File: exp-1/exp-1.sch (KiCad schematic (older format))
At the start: 15 parts

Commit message: Work continues on exp1
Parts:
- added C? (x7): .01u, symbol C
- added C? (x4): 470p, symbol C
- added C?: 15p, symbol C
- added D1: BAR15-1, Housings_SOT-23_SOT-143_TSOT-6:SOT-23, symbol DP2CA
- added FB? (x2): FILTER, symbol FILTER
- added FILT?: MTFILT, symbol MTFILT
- added L5, L? (x5): .33u, Resistors_SMD:R_0603, symbol INDUCTOR_C
- added R?: 680R, symbol R
- added R? (x2): 121R, symbol R
- added U?: ABA-52563, symbol ABA-52563
- added U?: AVT-50663, symbol AVT-50663
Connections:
- net labels added: RATT, VTX
- wire segments 24 -> 94
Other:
- note added: "NOTE: CONFIRM BIAS RESISTORS\n"
- note added: "RF BPF"
- note added: "SRSLY\n"
- moved on the sheet: C1, C10, C2, C3, C4, C5, C6, C7, C8, C9, FILT?, L1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

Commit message: More work done on copying DSP-10. Layout started.
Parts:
- added C23, C31, C38, C43: 470p, Capacitors_SMD:C_0603_HandSoldering, symbol C
- added C24, C25, C27, C32, C36, C39, C41, C44: .01u, Capacitors_SMD:C_0603_HandSoldering, symbol C
- added C26, C28, C30: 15p, Capacitors_SMD:C_0603_HandSoldering, symbol C
- added C29: 8.2p, Capacitors_SMD:C_0603_HandSoldering, symbol C
- added C33, C40: 47p, Capacitors_SMD:C_0603_HandSoldering, symbol C
- added C34, C37: 12p, Capacitors_SMD:C_0603_HandSoldering, symbol C
- added C35: 1p, Capacitors_SMD:C_0603_HandSoldering, symbol C
- added C42: 33p, Capacitors_SMD:C_0603_HandSoldering, symbol C
- added D2: BAR15-1, Housings_SOT-23_SOT-143_TSOT-6:SOT-23, symbol DP2CA
- added FILT3, FILT4: MTFILT, exp-1:FILTACH32T, symbol MTFILT
- added L11: 100n, Resistors_SMD:R_0603, symbol INDUCTOR_C
- added L12: 39n, Resistors_SMD:R_0603, symbol INDUCTOR
- added L13, L14, L15, L16, L17: .33u, Resistors_SMD:R_0603, symbol INDUCTOR_C
- added L18, L19: 100n, Resistors_SMD:R_0603, symbol INDUCTOR
- added P1, P2, P3: CONN_2, symbol CONN_2
- added Q1: 2n5109, Discret:TO39EBC, symbol NPN
- added R10, R11, R12: 331R, Resistors_SMD:R_0603_HandSoldering, symbol RA
- added R4: 3.3k, Resistors_SMD:R_0603_HandSoldering, symbol RA
- added R5: 1K, Resistors_SMD:R_0603_HandSoldering, symbol RA
- added R6: 2.2R, Resistors_SMD:R_0603_HandSoldering, symbol RA
- added R7: 22R, Resistors_SMD:R_0603_HandSoldering, symbol RA
- added R8: 680R, Resistors_SMD:R_0603_HandSoldering, symbol RA
- added R9: 121R, Resistors_SMD:R_0603_HandSoldering, symbol RA
- added U3: ABA-52563, exp-1:SOT_363, symbol ABA-52563
- added U4: AVT-50663, exp-1:SOT_363, symbol AVT-50663
- C1, C10, C2, C3, C4, C5, C6, C7, C8, C9: footprint Resistors_SMD:R_0603 -> Capacitors_SMD:C_0603_HandSoldering
- C11, C12, C13, C14, C15, C16, C17, C18, C19, C20, C21, C22: renamed from C?; footprint (none) -> Capacitors_SMD:C_0603_HandSoldering
- FB1, FB2: renamed from FB?; footprint (none) -> Choke_SMD:Choke_SMD_1206_Handsoldering
- FILT1, FILT2: renamed from FILT?; footprint (none) -> exp-1:FILTACH32T
- R1, R2: renamed from R?; footprint (none) -> Resistors_SMD:R_0603_HandSoldering; symbol R -> RA
- R3: renamed from R?; value 121R -> 331R; footprint (none) -> Resistors_SMD:R_0603_HandSoldering; symbol R -> RA
- U1, U2: renamed from U?; footprint (none) -> exp-1:SOT_363
- gave numbers to parts that had none: 5
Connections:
- net labels added: RATT2, RATT_1, TX_P, VRX
- net labels removed: RATT
- wire segments 94 -> 220
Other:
- moved on the sheet: C1, C10, C11, C12, C13, C14, C15, C16, C17, C18, C19, C2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

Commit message: Continued work on radio project thing
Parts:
- removed C20: 470p, Capacitors_SMD:C_0603_HandSoldering, symbol C
- removed C22: .01u, Capacitors_SMD:C_0603_HandSoldering, symbol C
- removed FILT2: MTFILT, exp-1:FILTACH32T, symbol MTFILT
- removed L10: .33u, Resistors_SMD:R_0603, symbol INDUCTOR_C
- removed P1: CONN_2, symbol CONN_2
- added SL?: SDRSEL, symbol SDRSEL
- added U?: ADE-1, symbol ADE-1
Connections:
- net GND: now also U?.1, U?.4, U?.5
- net TX_P: now also SL?.1; no longer P3.1 (P1)
- net at C10.1: now also U?.3 (RF)
- net at D2.1, L13.1: now also C31.2; no longer C31.1
- new net: P3.1 (P1), SL?.2
- new net IF: U?.2 (IF)
- new net LO: U?.6 (LO)
- new net TX_SL: C31.1, SL?.3
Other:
- moved on the sheet: C1, C10, C11, C12, C13, C14, C15, C16, C17, C18, C19, C2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

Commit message: Further work on radio thing
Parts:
- added U?: Si570, symbol Si570
- SL1: renamed from SL?; footprint (none) -> exp-1:BSEL2
- U5: renamed from U?; footprint (none) -> exp-1:PL-052
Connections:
- net GND: now also U?.3 (GND)
- new net +3.3V: U?.6 (VCC)

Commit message: Finished first round of routing. Power circuitry and breakout still needed.
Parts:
- added C20, C22: .01u, Capacitors_SMD:C_0603_HandSoldering, symbol C
- added C45, C46: 470p, Capacitors_SMD:C_0603_HandSoldering, symbol C
- added R13, R14: 1K, Resistors_SMD:R_0603_HandSoldering, symbol RA
- added R15: 38R, Resistors_SMD:R_0603_HandSoldering, symbol RA
- U6: renamed from U?; footprint (none) -> exp-1:SI570-HS
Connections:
- net +3.3V: now also U6.2 (OE), C20.1, C22.1, R13.2, R14.2
- net GND: now also C20.2, C22.2
- net IF: now also C46.1; no longer U5.2 (IF)
- net LO: now also C45.1
- net at C39.1, FILT4.1, R10.2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: no longer C41.1, L16.1, R9.2, U3.4 (VCC)
- net at U6.4 (CLK+): now also R15.2
- net SDA: now reaches U6.7 (SDA)
- net SDA: now also R14.1
- net SCL: now reaches U6.8 (SCL)
- net SCL: now also R13.1
- new net: C41.1, L16.1, R9.2, U3.4 (VCC)
- new net: C45.2, R15.1
- new net: C46.2, U5.2 (IF)
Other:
- note removed: "NOTE: CONFIRM BIAS RESISTORS\n"
- note removed: "SRSLY\n"
- moved on the sheet: U6

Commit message: Some more radio work
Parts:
- added Q? (x2): DMP3099L, symbol MOSFET_P
- added Q?: MMBT3904T, symbol NPN
- added Q?: NPN, symbol NPN
- added R? (x4): 10K, symbol RA
- added R? (x2): 1K, symbol RA
- added U?: LM2937, symbol LM2937
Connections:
- net GND: now also Q?.1 (E), Q?.1 (E), R?.1, R?.1, U?.2 (GND)
- net VRX: now also Q?.S
- net VTX: now also Q?.S
- new net: Q?.3 (C), Q?.G, R?.2 (x2)
- new net: Q?.2 (B), R?.2, R?.2 (x2)
- new net 10V: Q?.D, Q?.D, R?.1, R?.1, U?.3 (VO)
- new net EN_RX: R?.1
- new net EN_TX: R?.1
- new net VIN: U?.1 (VI)
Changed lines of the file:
@@
 Wire Wire Line
 	4300 5350 4600 5350
+$Comp
+L MOSFET_P Q?
+U 1 1 551F46EA
+P 2550 3500
+F 0 "Q?" H 2550 3690 60  0000 R CNN
+F 1 "DMP3099L" H 3150 3550 60  0000 R CNN
+F 2 "" H 2550 3500 60  0000 C CNN
+F 3 "" H 2550 3500 60  0000 C CNN
+	1    2550 3500
+	1    0    0    -1
+$EndComp
+$Comp
+L MOSFET_P Q?
+U 1 1 551F47CB
+P 4450 3500
+F 0 "Q?" H 4450 3690 60  0000 R CNN
+F 1 "DMP3099L" H 5050 3550 60  0000 R CNN
+F 2 "" H 4450 3500 60  0000 C CNN
+F 3 "" H 4450 3500 60  0000 C CNN
+	1    4450 3500
+	1    0    0    -1
+$EndComp
+$Comp
+L NPN Q?
+U 1 1 551F52D8
+P 2100 3750
+F 0 "Q?" H 2100 3600 50  0000 R CNN
+F 1 "MMBT3904T" H 2100 3900 50  0000 R CNN
+F 2 "" H 2100 3750 60  0000 C CNN
+F 3 "" H 2100 3750 60  0000 C CNN
+	1    2100 3750
+	1    0    0    -1
+$EndComp
+$Comp
+L NPN Q?
+U 1 1 551F5992
+P 4000 3750
+F 0 "Q?" H 4000 3600 50  0000 R CNN
+F 1 "NPN" H 4000 3900 50  0000 R CNN
+F 2 "" H 4000 3750 60  0000 C CNN
+F 3 "" H 4000 3750 60  0000 C CNN
+	1    4000 3750
+	1    0    0    -1
+$EndComp
+Wire Wire Line
+	2200 3400 2200 3550
+Wire Wire Line
+	2200 3500 2350 3500
+Wire Wire Line
+	4100 3400 4100 3550
+Wire Wire Line
+	4100 3500 4250 3500
+Wire Wire Line
+	2200 3950 2200 4250
+Wire Wire Line
+	4100 3950 4100 4250
+Text Label 1100 3750 0    60   ~ 0
+EN_RX
+Text Label 3050 3750 0    60   ~ 0
+EN_TX
+$Comp
+L GND #PWR?
+U 1 1 551F7A1C
+P 2000 4300
+F 0 "#PWR?" H 2000 4300 30  0001 C CNN
+F 1 "GND" H 2000 4230 30  0001 C CNN
+F 2 "" H 2000 4300 60  0000 C CNN
+F 3 "" H 2000 4300 60  0000 C CNN
+	1    2000 4300
+	1    0    0    -1
+$EndComp
+$Comp
+L GND #PWR?
+U 1 1 551F7C1B
+P 3950 4300
+F 0 "#PWR?" H 3950 4300 30  0001 C CNN
+F 1 "GND" H 3950 4230 30  0001 C CNN
+F 2 "" H 3950 4300 60  0000 C CNN
+F 3 "" H 3950 4300 60  0000 C CNN
+	1    3950 4300
+	1    0    0    -1
+$EndComp
+Wire Wire Line
+	2650 2950 2650 3300
+Wire Wire Line
+	4550 2950 4550 3300
+Wire Wire Line
+	4550 3700 4550 3800
+Wire Wire Line
+	4550 3800 4850 3800
+Wire Wire Line
+	2650 3700 2650 3800
+Wire Wire Line
+	2650 3800 2850 3800
+Text Label 2850 3800 2    60   ~ 0
+VRX
+Text Label 4850 3800 2    60   ~ 0
+VTX
+$Comp
+L RA R?
+U 1 1 551F90B9
+P 4100 3250
+F 0 "R?" V 4180 3300 40  0000 C CNN
+F 1 "10K" V 4000 3300 40  0000 C CNN
+F 2 "" V 4030 3300 30  0000 C CNN
+F 3 "" H 4100 3300 30  0000 C CNN
+	1    4100 3250
+	1    0    0    -1
+$EndComp
+$Comp
+L RA R?
+U 1 1 551F943E
+P 2200 3250
+F 0 "R?" V 2280 3300 40  0000 C CNN
+F 1 "10K" V 2100 3300 40  0000 C CNN
+F 2 "" V 2130 3300 30  0000 C CNN
+F 3 "" H 2200 3300 30  0000 C CNN
+	1    2200 3250
+	1    0    0    -1
+$EndComp
+Connection ~ 2200 3500
+Connection ~ 4100 3500
+Wire Wire Line
+	2200 3050 2200 2950
+Wire Wire Line
+	2200 2950 2650 2950
+Wire Wire Line
+	4100 3050 4100 2950
+Wire Wire Line
+	4100 2950 4550 2950
+Text Label 2200 2950 0    60   ~ 0
+10V
+Text Label 4100 2950 0    60   ~ 0
+10V
+$Comp
+L RA R?
+U 1 1 551FAA15
+P 1850 4000
+F 0 "R?" V 1930 4050 40  0000 C CNN
+F 1 "10K" V 1750 4050 40  0000 C CNN
+F 2 "" V 1780 4050 30  0000 C CNN
+F 3 "" H 1850 4050 30  0000 C CNN
+	1    1850 4000
+	-1   0    0    1
+$EndComp
+$Comp
+L RA R?
+U 1 1 551FAC2D
+P 1600 3750
+F 0 "R?" V 1680 3800 40  0000 C CNN
+F 1 "1K" V 1500 3800 40  0000 C CNN
+F 2 "" V 1530 3800 30  0000 C CNN
+F 3 "" H 1600 3800 30  0000 C CNN
+	1    1600 3750
+	0    -1   -1   0
+$EndComp
+Wire Wire Line
+	1750 3750 1900 3750
+Wire Wire Line
+	1850 3750 1850 3850
+Connection ~ 1850 3750
+Wire Wire Line
+	1850 4200 1850 4250
+Wire Wire Line
+	1850 4250 2200 4250
+Wire Wire Line
+	3950 4250 3950 4300
+Connection ~ 3950 4250
+Wire Wire Line
+	2000 4250 2000 4300
+Connection ~ 2000 4250
+$Comp
+L RA R?
+U 1 1 551FCF6E
+P 3750 4000
+F 0 "R?" V 3830 4050 40  0000 C CNN
+F 1 "10K" V 3650 4050 40  0000 C CNN
+F 2 "" V 3680 4050 30  0000 C CNN
+F 3 "" H 3750 4050 30  0000 C CNN
+	1    3750 4000
+	-1   0    0    1
+$EndComp
+$Comp
+L RA R?
+U 1 1 551FCF74
+P 3500 3750
+F 0 "R?" V 3580 3800 40  0000 C CNN
+F 1 "1K" V 3400 3800 40  0000 C CNN
+F 2 "" V 3430 3800 30  0000 C CNN
+F 3 "" H 3500 3800 30  0000 C CNN
+	1    3500 3750
+	0    -1   -1   0
+$EndComp
+Wire Wire Line
+	3650 3750 3800 3750
+Wire Wire Line
+	3750 3750 3750 3850
+Connection ~ 3750 3750
+Wire Wire Line
+	3750 4200 3750 4250
+Wire Wire Line
+	3750 4250 4100 4250
+Wire Wire Line
+	1100 3750 1400 3750
+Wire Wire Line
+	3050 3750 3300 3750
+$Comp
+L LM2937 U?
+U 1 1 552001A0
+P 6850 2750
+F 0 "U?" H 7000 2554 60  0000 C CNN
+F 1 "LM2937" H 6850 2950 60  0000 C CNN
+F 2 "" H 6850 2750 60  0000 C CNN
+F 3 "" H 6850 2750 60  0000 C CNN
+	1    6850 2750
+	1    0    0    -1
+$EndComp
+$Comp
+L GND #PWR?
+U 1 1 5520080E
+P 6850 3100
+F 0 "#PWR?" H 6850 3100 30  0001 C CNN
+F 1 "GND" H 6850 3030 30  0001 C CNN
+F 2 "" H 6850 3100 60  0000 C CNN
+F 3 "" H 6850 3100 60  0000 C CNN
+	1    6850 3100
+	1    0    0    -1
+$EndComp
+Wire Wire Line
+	6850 3000 6850 3100
+Wire Wire Line
+	6150 2700 6450 2700
+Text Label 6150 2700 0    60   ~ 0
+VIN
+Wire Wire Line
+	7250 2700 7600 2700
+Text Label 7350 2700 0    60   ~ 0
+10V
 $EndSCHEMATC

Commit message: just commit-n'
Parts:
- added D?: DIODESCH, symbol DIODESCH
- added Q?: DMP3099L, symbol MOSFET_P
- added Q?: MMBT3904T, symbol NPN
- added R? (x2): 10K, symbol RA
- added R?: 1K, symbol RA
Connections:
- net 10V: now also Q?.S, Q?.S; no longer Q?.D, Q?.D
- net EN_RX: now also R?.1
- net GND: now also Q?.1 (E), R?.1
- net VRX: now also Q?.D; no longer Q?.S
- net VTX: now also Q?.D; no longer Q?.S
- net at Q?.2 (B), R?.2, R?.2: now also D?.1 (A)
- new net: D?.2 (K), Q?.3 (C), Q?.G, R?.2
- new net: Q?.S, R?.1
- new net: Q?.2 (B), R?.2, R?.2
- new net VATT: Q?.D
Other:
- note added: "Antenna side TX/RX Switch\nand RX attenuator"
- note added: "Local Oscillator"
- note added: "Mixer"
- note added: "Mixer side TX/RX Switch\nand RX attenuator"
- note added: "Power to TX/RX stages and attenuator"
- note added: "RX Amplifier"
- note added: "RX BPF"
- note added: "TX amplifier and LPF"
- note added: "TX/RX "lockout""
- moved on the sheet: Q?, R?, U?

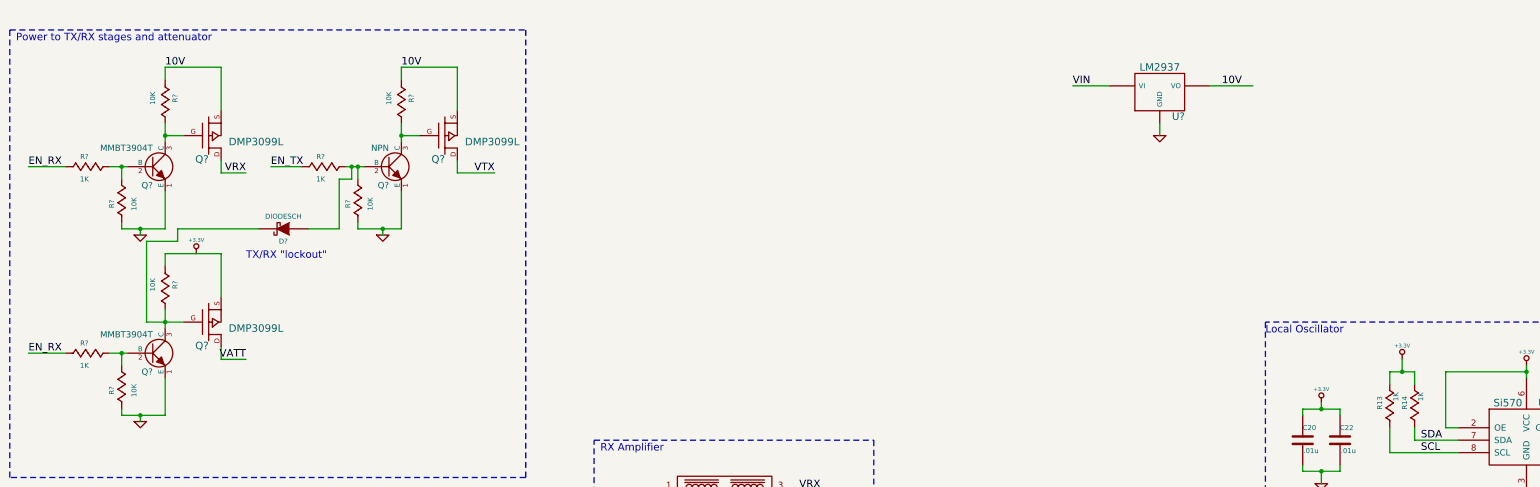
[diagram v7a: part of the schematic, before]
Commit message: Further work on radio. Added attenuator biasing.
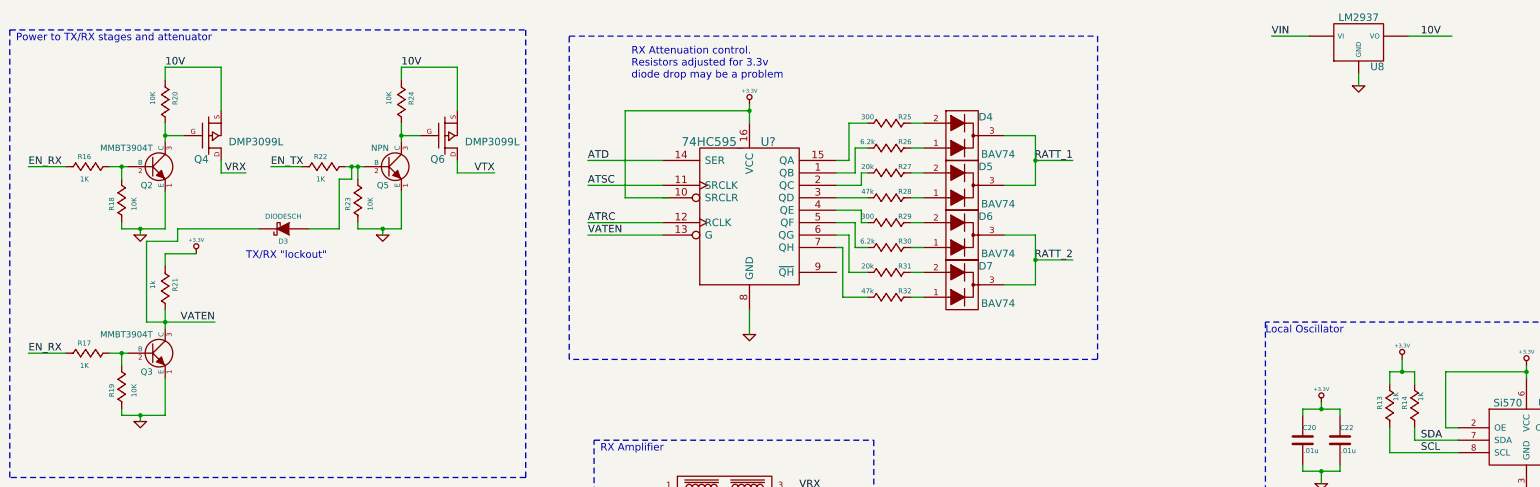
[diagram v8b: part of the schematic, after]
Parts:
- removed Q?: DMP3099L, symbol MOSFET_P
- added D4, D5, D6, D7: BAV74, Housings_SOT-23_SOT-143_TSOT-6:SOT-23, symbol DP2CA
- added R25, R29: 300, symbol RA
- added R26, R30: 6.2k, symbol RA
- added R27, R31: 20k, symbol RA
- added R28, R32: 47k, symbol RA
- added U?: 74HC595_, symbol 74HC595_
- R21: renamed from R?; value 10K -> 1k
- gave numbers to parts that had none: 15
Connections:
- net +3.3V: now also R21.1, U?.16 (VCC)
- net GND: now also U?.8 (GND)
- net RATT_1: now also D4.3, D5.3
- net VATEN: now reaches D3.2 (K), Q3.3 (C), R21.2
- net VATEN: now also U?.13 (G)
- new net: D4.2, R25.1
- new net: R25.2, U?.15 (QA)
- new net: D4.1, R26.1
- new net: R26.2, U?.1 (QB)
- new net: D5.2, R27.1
- new net: R27.2, U?.2 (QC)
- new net: D5.1, R28.1
- new net: R28.2, U?.3 (QD)
- new net: D6.2, R29.1
- new net: R29.2, U?.4 (QE)
- new net: D6.1, R30.1
- new net: R30.2, U?.5 (QF)
- new net: D7.2, R31.1
- new net: R31.2, U?.6 (QG)
- new net: D7.1, R32.1
- new net: R32.2, U?.7 (QH)
- new net ATD: U?.14 (SER)
- new net ATRC: U?.12 (RCLK)
- new net ATSC: U?.11 (SRCLK)
- new net RATT_2: D6.3, D7.3
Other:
- note added: "RX Attenuation control.\nResistors adjusted for 3.3v\ndiode drop may be a problem"
- moved on the sheet: U8
